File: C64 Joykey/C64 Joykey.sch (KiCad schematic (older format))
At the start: 30 parts, among them J1 Port_1, J2 Port_2, M1 Mounting, M2 Mounting, M3 Mounting, M4 Mounting, SW1 FIRE1, SW2 FIRE2, SW3 FIRE3, SW4 UP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

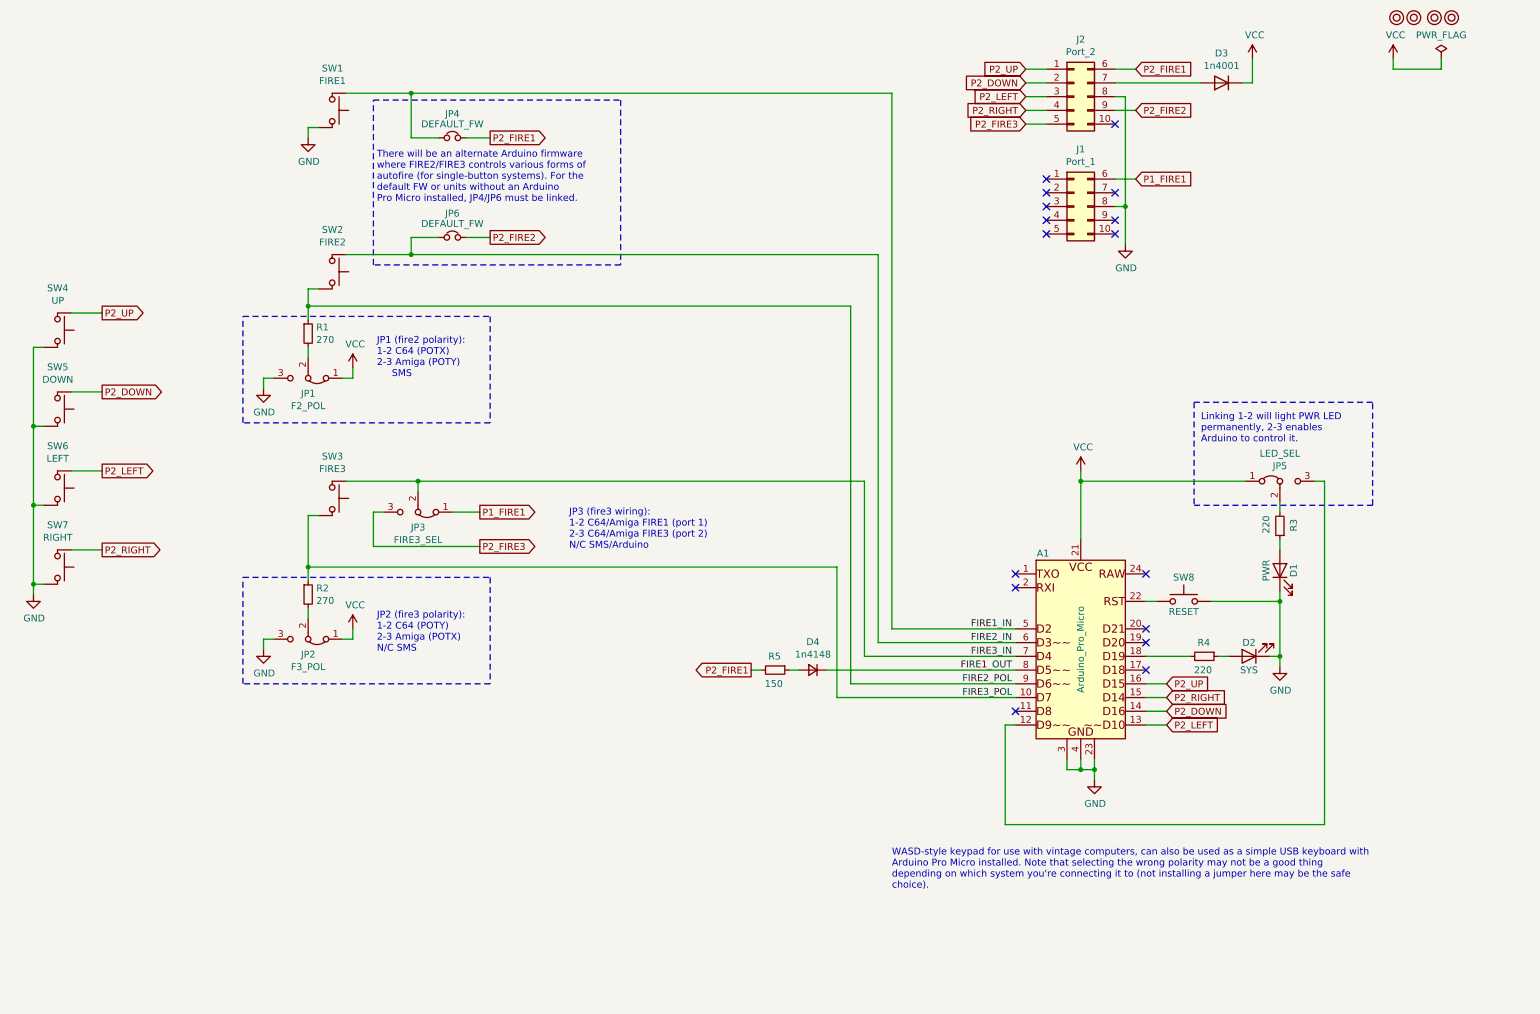
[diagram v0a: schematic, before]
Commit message: Underglow LEDs added
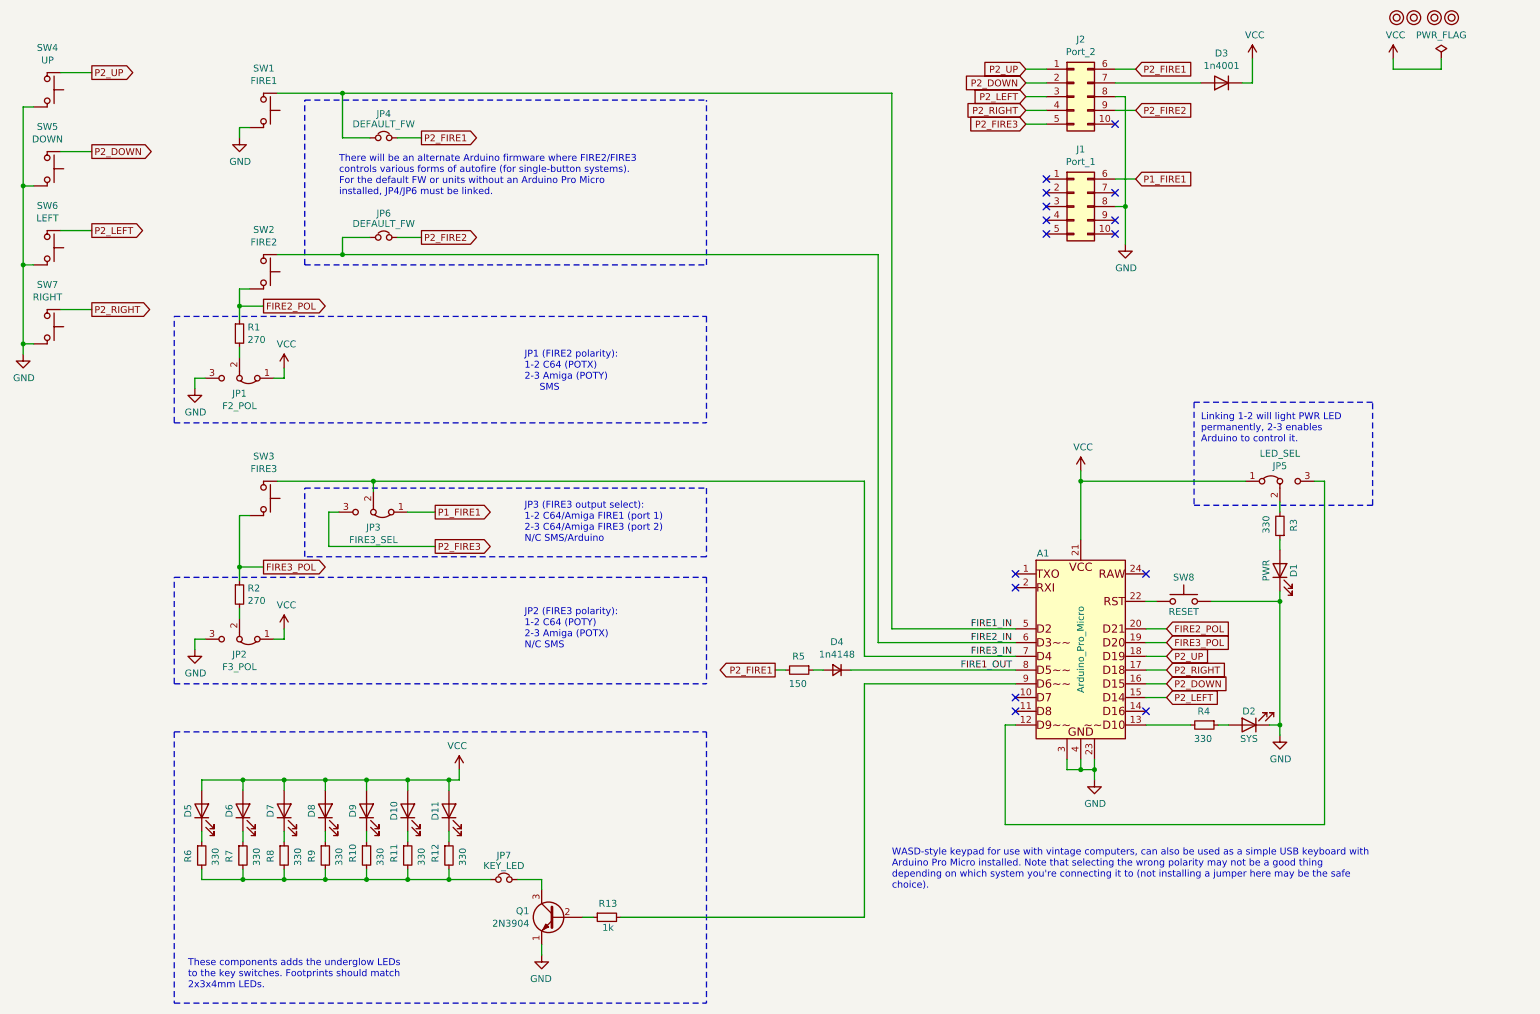
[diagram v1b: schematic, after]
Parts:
- added D10, D11, D5, D6, D7, D8, D9: LED, LED_THT:LED_Rectangular_W3.0mm_H2.0mm, symbol Device:LED
- added JP7: KEY_LED, Connector_PinHeader_2.54mm:PinHeader_1x02_P2.54mm_Horizontal, symbol Device:Jumper_NC_Small
- added Q1: 2N3904, Package_TO_SOT_THT:TO-92_Inline_W4.0mm_Horizontal_FlatSideDown, symbol Transistor_BJT:2N3904
- added R10, R11, R12, R6, R7, R8, R9: 330, Resistor_THT:R_Axial_DIN0207_L6.3mm_D2.5mm_P10.16mm_Horizontal, symbol Device:R_Small
- added R13: 1k, Resistor_THT:R_Axial_DIN0207_L6.3mm_D2.5mm_P10.16mm_Horizontal, symbol Device:R_Small
- JP4, JP6: footprint Pin_Headers:Pin_Header_Straight_1x02_Pitch2.54mm -> Connector_PinHeader_2.54mm:PinHeader_1x02_P2.54mm_Vertical
- R1, R2: footprint Resistors_THT:R_Axial_DIN0207_L6.3mm_D2.5mm_P10.16mm_Horizontal -> Resistor_THT:R_Axial_DIN0207_L6.3mm_D2.5mm_P10.16mm_Horizontal
- R3, R4: value 220 -> 330; footprint Resistors_THT:R_Axial_DIN0207_L6.3mm_D2.5mm_P10.16mm_Horizontal -> Resistor_THT:R_Axial_DIN0207_L6.3mm_D2.5mm_P10.16mm_Horizontal
- R5: footprint Resistors_THT:R_Axial_DIN0207_L6.3mm_D2.5mm_P7.62mm_Horizontal -> Resistor_THT:R_Axial_DIN0207_L6.3mm_D2.5mm_P7.62mm_Horizontal
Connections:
- net FIRE2_POL: now also A1.20 (D21); no longer A1.9 (D6)
- net FIRE3_POL: now also A1.19 (D20); no longer A1.10 (D7)
- net GND: now also Q1.1 (E)
- net P2_DOWN: now also A1.16 (D15); no longer A1.14 (D16)
- net P2_LEFT: now also A1.15 (D14); no longer A1.13 (D10)
- net P2_RIGHT: now also A1.17 (D18); no longer A1.15 (D14)
- net P2_UP: now also A1.18 (D19); no longer A1.16 (D15)
- net VCC: now also D10.2 (A), D11.2 (A), D5.2 (A), D6.2 (A), D7.2 (A), D8.2 (A), D9.2 (A)
- net at R4.2: now also A1.13 (D10); no longer A1.18 (D19)
- new net: A1.9 (D6), R13.2
- new net: D11.1 (K), R12.1
- new net: Q1.2 (B), R13.1
- new net: JP7.2, Q1.3 (C)
- new net: D10.1 (K), R11.1
- new net: D9.1 (K), R10.1
- new net: D8.1 (K), R9.1
- new net: D7.1 (K), R8.1
- new net: D6.1 (K), R7.1
- new net: D5.1 (K), R6.1
- new net: JP7.1, R10.2, R11.2, R12.2, R6.2, R7.2, R8.2, R9.2
- no-connect marks 16 -> 15
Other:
- note added: "JP1 (FIRE2 polarity):\n1-2 C64 (POTX)\n2-3 Amiga (POTY)\n SMS\n"
- note added: "JP2 (FIRE3 polarity):\n1-2 C64 (POTY)\n2-3 Amiga (POTX)\nN/C SMS\n"
- note added: "JP3 (FIRE3 output select):\n1-2 C64/Amiga FIRE1 (port 1)\n2-3 C64/Amiga FIRE3 (port 2)\nN/C SMS/Arduino"
- note added: "There will be an alternate Arduino firmware where FIRE2/FIRE3\ncontrols various forms of autofire (for single-button systems).\nFor the default FW or units without an Arduino Pro Micro \ninstalled, JP4/JP6 must be linked."
- note added: "These components adds the underglow LEDs\nto the key switches. Footprints should match\n2x3x4mm LEDs."
- note removed: "JP1 (fire2 polarity):\n1-2 C64 (POTX)\n2-3 Amiga (POTY)\n SMS\n"
- note removed: "JP2 (fire3 polarity):\n1-2 C64 (POTY)\n2-3 Amiga (POTX)\nN/C SMS\n"
- note removed: "JP3 (fire3 wiring):\n1-2 C64/Amiga FIRE1 (port 1)\n2-3 C64/Amiga FIRE3 (port 2)\nN/C SMS/Arduino"
- note removed: "There will be an alternate Arduino firmware\nwhere FIRE2/FIRE3 controls various forms of\nautofire (for single-button systems). For the\ndefault FW or units without an Arduino\nPro Micro installed, JP4/JP6 must be linked."
- moved on the sheet: D2, D4, JP1, JP2, JP3, JP4, JP6, R1, R2, R4, R5, SW1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

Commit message: Changed Q1 footprint
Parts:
- Q1: footprint Package_TO_SOT_THT:TO-92_Inline_W4.0mm_Horizontal_FlatSideDown -> 2n3904:2N3904_TO-92_Horizontal_FlatSideDown
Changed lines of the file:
@@
 F 0 "Q1" H 4765 7146 50  0000 L CNN
 F 1 "2N3904" H 4765 7055 50  0000 L CNN
-F 2 "Package_TO_SOT_THT:TO-92_Inline_W4.0mm_Horizontal_FlatSideDown" H 4775 7025 50  0001 L CIN
+F 2 "2n3904:2N3904_TO-92_Horizontal_FlatSideDown" H 4775 7025 50  0001 L CIN
 F 3 "https://www.onsemi.com/pub/Collateral/2N3903-D.PDF" H 4575 7100 50  0001 L CNN
 	1    4575 7100

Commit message: Flipped MX-switches
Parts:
- added D12: 1n4148, Diode_THT:D_DO-35_SOD27_P7.62mm_Horizontal, symbol Device:D_Small
- added R14: 150, Resistor_THT:R_Axial_DIN0207_L6.3mm_D2.5mm_P10.16mm_Horizontal, symbol Device:R_Small
- D4: footprint Diodes_THT:D_DO-35_SOD27_P7.62mm_Horizontal -> Diode_THT:D_DO-35_SOD27_P7.62mm_Horizontal
- J1: symbol Connector_Generic:Conn_02x05_Top_Bottom -> c64_idc:C64_IDC2_OUT
- J2: symbol c64_idc:c64_idc -> c64_idc:C64_IDC2_OUT
- R5: footprint Resistor_THT:R_Axial_DIN0207_L6.3mm_D2.5mm_P7.62mm_Horizontal -> Resistor_THT:R_Axial_DIN0207_L6.3mm_D2.5mm_P10.16mm_Horizontal
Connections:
- net P2_FIRE2: now also R14.2
- net FIRE2_OUT: now reaches A1.10 (D7)
- net FIRE2_OUT: now also D12.1 (K)
- net PWR: now reaches A1.12 (D9), JP5.3 (B)
- net SYS: now reaches A1.13 (D10), R4.2
- net UNDERGLOW: now reaches A1.9 (D6), R13.2
- new net: D12.2 (A), R14.1
- no-connect marks 15 -> 12
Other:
- note added: "These components adds the underglow LEDs to the key\nswitches. Footprints should match 2x3x4mm LEDs.\nStandard 3mm should also work with Gateron switches."
- note removed: "These components adds the underglow LEDs\nto the key switches. Footprints should match\n2x3x4mm LEDs."
- moved on the sheet: D3
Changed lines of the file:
@@
 	2275 1350 2350 1350
 $Comp
-L Connector_Generic:Conn_02x05_Top_Bottom J1
+L c64_idc:C64_IDC2_OUT J1
 U 1 1 5FB76154
-P 8350 1925
-F 0 "J1" H 8400 2342 50  0000 C CNN
-F 1 "Port_1" H 8400 2251 50  0000 C CNN
-F 2 "C64 IDC:IDC_Joystick" H 8350 1925 50  0001 C CNN
-F 3 "~" H 8350 1925 50  0001 C CNN
-	1    8350 1925
+P 8350 2200
+F 0 "J1" H 8400 2617 50  0000 C CNN
+F 1 "Port_1" H 8400 2526 50  0000 C CNN
+F 2 "C64 IDC:IDC_Joystick" H 8350 2200 50  0001 C CNN
+F 3 "~" H 8350 2200 50  0001 C CNN
+	1    8350 2200
 	1    0    0    -1
 $EndComp
@@
 L power:GND #PWR03
 U 1 1 5FB76300
-P 8725 2200
-F 0 "#PWR03" H 8725 1950 50  0001 C CNN
-F 1 "GND" H 8730 2027 50  0000 C CNN
-F 2 "" H 8725 2200 50  0001 C CNN
-F 3 "" H 8725 2200 50  0001 C CNN
-	1    8725 2200
-	1    0    0    -1
-$EndComp
-NoConn ~ 8650 1325
-NoConn ~ 8650 2125
-Wire Wire Line
-	8650 1725 8800 1725
-Text GLabel 8800 925  2    50   Input ~ 0
+P 8900 2475
+F 0 "#PWR03" H 8900 2225 50  0001 C CNN
+F 1 "GND" H 8905 2302 50  0000 C CNN
+F 2 "" H 8900 2475 50  0001 C CNN
+F 3 "" H 8900 2475 50  0001 C CNN
+	1    8900 2475
+	1    0    0    -1
+$EndComp
+Wire Wire Line
+	8825 2000 8975 2000
+Text GLabel 8975 1200 2    50   Input ~ 0
 P2_FIRE1
-Text GLabel 8800 1725 2    50   Input ~ 0
+Text GLabel 8975 2000 2    50   Input ~ 0
 P1_FIRE1
 $Comp
 L power:VCC #PWR02
 U 1 1 5FB781A5
-P 9650 850
-F 0 "#PWR02" H 9650 700 50  0001 C CNN
-F 1 "VCC" H 9667 1023 50  0000 C CNN
-F 2 "" H 9650 850 50  0001 C CNN
-F 3 "" H 9650 850 50  0001 C CNN
-	1    9650 850
-	1    0    0    -1
-$EndComp
-NoConn ~ 8150 1725
-NoConn ~ 8150 1825
-NoConn ~ 8150 1925
-NoConn ~ 8150 2025
-NoConn ~ 8150 2125
-NoConn ~ 8650 1825
-Text GLabel 8000 925  0    50   Input ~ 0
+P 9825 1125
+F 0 "#PWR02" H 9825 975 50  0001 C CNN
+F 1 "VCC" H 9842 1298 50  0000 C CNN
+F 2 "" H 9825 1125 50  0001 C CNN
+F 3 "" H 9825 1125 50  0001 C CNN
+	1    9825 1125
+	1    0    0    -1
+$EndComp
+NoConn ~ 7900 2000
+NoConn ~ 7900 2100
+NoConn ~ 7900 2200
+NoConn ~ 7900 2300
+NoConn ~ 7900 2400
+NoConn ~ 8825 2100
+Text GLabel 7750 1200 0    50   Input ~ 0
 P2_UP
 Wire Wire Line
-	8000 925  8150 925
-Text GLabel 8000 1025 0    50   Input ~ 0
+	7750 1200 7900 1200
+Text GLabel 7750 1300 0    50   Input ~ 0
 P2_DOWN
 Wire Wire Line
-	8150 1025 8000 1025
-Text GLabel 8000 1125 0    50   Input ~ 0
+	7900 1300 7750 1300
+Text GLabel 7750 1400 0    50   Input ~ 0
 P2_LEFT
 Wire Wire Line
-	8000 1125 8150 1125
-Text GLabel 8000 1225 0    50   Input ~ 0
+	7750 1400 7900 1400
+Text GLabel 7750 1500 0    50   Input ~ 0
 P2_RIGHT
 Wire Wire Line
-	8000 1225 8150 1225
-Text GLabel 8800 1225 2    50   Input ~ 0
+	7750 1500 7900 1500
+Text GLabel 8975 1500 2    50   Input ~ 0
 P2_FIRE2
 Wire Wire Line
-	8800 1225 8650 1225
-Text GLabel 8000 1325 0    50   Input ~ 0
+	8975 1500 8825 1500
+Text GLabel 7750 1600 0    50   Input ~ 0
 P2_FIRE3
 Wire Wire Line
-	8000 1325 8150 1325
+	7750 1600 7900 1600
 $Comp
 L sw_keyboard:SW_Keyboard SW4
@@
 P2_FIRE1
 Wire Wire Line
-	8650 1925 8725 1925
-Connection ~ 8725 1925
-Wire Wire Line
-	8725 1925 8725 2200
-NoConn ~ 8650 2025
-Wire Wire Line
-	8650 1125 8725 1125
-Wire Wire Line
-	8725 1125 8725 1925
-Wire Wire Line
-	9650 1025 9650 850
+	8825 2200 8900 2200
+Connection ~ 8900 2200
+Wire Wire Line
+	8900 2200 8900 2475
+NoConn ~ 8825 2300
+Wire Wire Line
+	8825 1400 8900 1400
+Wire Wire Line
+	8900 1400 8900 2200
+Wire Wire Line
+	9825 1300 9825 1125
 Text GLabel 9025 5300 2    50   Input ~ 0
 P2_RIGHT
@@
 	8400 3925 9600 3925
 Wire Wire Line
-	7925 5700 7850 5700
-Wire Wire Line
-	7850 5700 7850 6425
-Wire Wire Line
-	7850 6425 10175 6425
-Wire Wire Line
 	10175 6425 10175 3925
 Wire Wire Line
@@
 L Device:D D3
 U 1 1 5FCFF93E
-P 9425 1025
-F 0 "D3" H 9425 809 50  0000 C CNN
-F 1 "1n4001" H 9425 900 50  0000 C CNN
-F 2 "Diodes_THT:D_DO-41_SOD81_P10.16mm_Horizontal" H 9425 1025 50  0001 C CNN
-F 3 "~" H 9425 1025 50  0001 C CNN
-	1    9425 1025
+P 9600 1300
+F 0 "D3" H 9600 1084 50  0000 C CNN
+F 1 "1n4001" H 9600 1175 50  0000 C CNN
+F 2 "Diodes_THT:D_DO-41_SOD81_P10.16mm_Horizontal" H 9600 1300 50  0001 C CNN
+F 3 "~" H 9600 1300 50  0001 C CNN
+	1    9600 1300
 	-1   0    0    1
 $EndComp
 Wire Wire Line
-	8650 925  8800 925
-Wire Wire Line
-	9575 1025 9650 1025
-Wire Wire Line
-	8650 1025 9275 1025
+	8825 1200 8975 1200
+Wire Wire Line
+	9750 1300 9825 1300
+Wire Wire Line
+	8825 1300 9450 1300
 $Comp
 L power:PWR_FLAG #FLG0101
@@
 U 1 1 5FD49B7F
 P 6625 5300
-F 0 "D4" H 6625 5095 50  0000 C CNN
-F 1 "1n4148" H 6625 5186 50  0000 C CNN
-F 2 "Diodes_THT:D_DO-35_SOD27_P7.62mm_Horizontal" V 6625 5300 50  0001 C CNN
+F 0 "D4" H 6625 5125 50  0000 C CNN
+F 1 "1n4148" H 6625 5200 50  0000 C CNN
+F 2 "Diode_THT:D_DO-35_SOD27_P7.62mm_Horizontal" V 6625 5300 50  0001 C CNN
 F 3 "~" V 6625 5300 50  0001 C CNN
 	1    6625 5300
@@
 U 1 1 5FDC0E14
 P 6350 5300
-F 0 "R5" V 6250 5250 50  0000 L CNN
-F 1 "150" V 6450 5225 50  0000 L CNN
-F 2 "Resistor_THT:R_Axial_DIN0207_L6.3mm_D2.5mm_P7.62mm_Horizontal" H 6350 5300 50  0001 C CNN
+F 0 "R5" V 6175 5250 50  0000 L CNN
+F 1 "150" V 6250 5225 50  0000 L CNN
+F 2 "Resistor_THT:R_Axial_DIN0207_L6.3mm_D2.5mm_P10.16mm_Horizontal" H 6350 5300 50  0001 C CNN
 F 3 "~" H 6350 5300 50  0001 C CNN
 	1    6350 5300
@@
 	6175 5300 6250 5300
 $Comp
-L c64_idc:c64_idc J2
+L c64_idc:C64_IDC2_OUT J2
 U 1 1 5FB748C4
-P 8350 1125
-F 0 "J2" H 8400 1542 50  0000 C CNN
-F 1 "Port_2" H 8400 1451 50  0000 C CNN
-F 2 "C64 IDC:IDC_Joystick" H 8350 1125 50  0001 C CNN
-F 3 "~" H 8350 1125 50  0001 C CNN
-	1    8350 1125
+P 8350 1400
+F 0 "J2" H 8400 1817 50  0000 C CNN
+F 1 "Port_2" H 8400 1726 50  0000 C CNN
+F 2 "C64 IDC:IDC_Joystick" H 8350 1400 50  0001 C CNN
+F 3 "~" H 8350 1400 50  0001 C CNN
+	1    8350 1400
 	1    0    0    -1
 $EndComp
@@
 Wire Wire Line
 	8875 5100 9025 5100
-NoConn ~ 7925 5500
 Wire Wire Line
 	6825 7100 6825 5400
@@
 	1800 5750 1800 7725
 Text Notes 1900 7625 0    50   ~ 0
-These components adds the underglow LEDs\nto the key switches. Footprints should match\n2x3x4mm LEDs.
+These components adds the underglow LEDs to the key\nswitches. Footprints should match 2x3x4mm LEDs.\nStandard 3mm should also work with Gateron switches.
 Wire Wire Line
 	3025 2275 6925 2275
@@
 Wire Wire Line
 	4300 6825 4475 6825
+Text GLabel 6175 5500 0    50   Output ~ 0
+P2_FIRE2
+$Comp
+L Device:D_Small D12
+U 1 1 600C6BE2
+P 6625 5500
+F 0 "D12" H 6625 5600 50  0000 C CNN
+F 1 "1n4148" H 6625 5675 50  0000 C CNN
+F 2 "Diode_THT:D_DO-35_SOD27_P7.62mm_Horizontal" V 6625 5500 50  0001 C CNN
+F 3 "~" V 6625 5500 50  0001 C CNN
+	1    6625 5500
+	-1   0    0    1
+$EndComp
+$Comp
+L Device:R_Small R14
+U 1 1 600C6BE8
+P 6350 5500
+F 0 "R14" V 6450 5450 50  0000 L CNN
+F 1 "150" V 6525 5425 50  0000 L CNN
+F 2 "Resistor_THT:R_Axial_DIN0207_L6.3mm_D2.5mm_P10.16mm_Horizontal" H 6350 5500 50  0001 C CNN
+F 3 "~" H 6350 5500 50  0001 C CNN
+	1    6350 5500
+	0    1    1    0
+$EndComp
+Wire Wire Line
+	6450 5500 6525 5500
+Wire Wire Line
+	6175 5500 6250 5500
+Wire Wire Line
+	6725 5500 7925 5500
+Text Label 7900 5500 2    50   ~ 0
+FIRE2_OUT
+Text Label 8900 5700 0    50   ~ 0
+SYS
+Text Label 7900 5700 2    50   ~ 0
+PWR
+Wire Wire Line
+	7700 5700 7700 6425
+Wire Wire Line
+	7700 5700 7925 5700
+Wire Wire Line
+	7700 6425 10175 6425
+Text Label 7900 5400 2    50   ~ 0
+UNDERGLOW
 $EndSCHEMATC

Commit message: Added VCC_EN jumper
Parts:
- added JP8: VCC_EN, Connector_PinHeader_2.54mm:PinHeader_1x02_P2.54mm_Vertical, symbol Device:Jumper_NC_Small
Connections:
- net at J2.7 (Pin_7): now also JP8.1; no longer D3.2 (A)
- new net: D3.2 (A), JP8.2
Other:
- moved on the sheet: D3
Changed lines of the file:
@@
 L power:VCC #PWR02
 U 1 1 5FB781A5
-P 9825 1125
-F 0 "#PWR02" H 9825 975 50  0001 C CNN
-F 1 "VCC" H 9842 1298 50  0000 C CNN
-F 2 "" H 9825 1125 50  0001 C CNN
-F 3 "" H 9825 1125 50  0001 C CNN
-	1    9825 1125
+P 10325 1125
+F 0 "#PWR02" H 10325 975 50  0001 C CNN
+F 1 "VCC" H 10342 1298 50  0000 C CNN
+F 2 "" H 10325 1125 50  0001 C CNN
+F 3 "" H 10325 1125 50  0001 C CNN
+	1    10325 1125
 	1    0    0    -1
 $EndComp
@@
 	8900 1400 8900 2200
 Wire Wire Line
-	9825 1300 9825 1125
+	10325 1300 10325 1125
 Text GLabel 9025 5300 2    50   Input ~ 0
 P2_RIGHT
@@
 L Device:D D3
 U 1 1 5FCFF93E
-P 9600 1300
-F 0 "D3" H 9600 1084 50  0000 C CNN
-F 1 "1n4001" H 9600 1175 50  0000 C CNN
-F 2 "Diodes_THT:D_DO-41_SOD81_P10.16mm_Horizontal" H 9600 1300 50  0001 C CNN
-F 3 "~" H 9600 1300 50  0001 C CNN
-	1    9600 1300
+P 10100 1300
+F 0 "D3" H 10100 1084 50  0000 C CNN
+F 1 "1n4001" H 10100 1175 50  0000 C CNN
+F 2 "Diodes_THT:D_DO-41_SOD81_P10.16mm_Horizontal" H 10100 1300 50  0001 C CNN
+F 3 "~" H 10100 1300 50  0001 C CNN
+	1    10100 1300
 	-1   0    0    1
 $EndComp
@@
 	8825 1200 8975 1200
 Wire Wire Line
-	9750 1300 9825 1300
-Wire Wire Line
-	8825 1300 9450 1300
+	10250 1300 10325 1300
 $Comp
 L power:PWR_FLAG #FLG0101
@@
 Text Label 7900 5400 2    50   ~ 0
 UNDERGLOW
+$Comp
+L Device:Jumper_NC_Small JP8
+U 1 1 601EE585
+P 9675 1300
+F 0 "JP8" H 9675 1475 50  0000 C CNN
+F 1 "VCC_EN" H 9675 1400 50  0000 C CNN
+F 2 "Connector_PinHeader_2.54mm:PinHeader_1x02_P2.54mm_Vertical" H 9675 1300 50  0001 C CNN
+F 3 "~" H 9675 1300 50  0001 C CNN
+	1    9675 1300
+	1    0    0    -1
+$EndComp
+Wire Wire Line
+	9950 1300 9775 1300
+Wire Wire Line
+	8825 1300 9575 1300
 $EndSCHEMATC

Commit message: Added ARD_EN jumper
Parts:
- added JP9: ARD_EN, Connector_PinHeader_2.54mm:PinHeader_1x02_P2.54mm_Vertical, symbol Device:Jumper_NC_Small
- J2: symbol c64_idc:C64_IDC2_OUT -> c64_idc:C64_IDC2
- JP8: symbol Device:Jumper_NC_Small -> promicro:VCC_EN
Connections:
- net VCC: now also JP9.2; no longer A1.21 (VCC)
- new net: A1.21 (VCC), JP9.1
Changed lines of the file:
@@
 Wire Wire Line
 	8400 3925 8400 3850
-Connection ~ 8400 3925
 $Comp
 L Device:LED D2
@@
 	9850 4725 9850 4800
 Wire Wire Line
-	8400 3925 8400 4350
-Wire Wire Line
 	8400 3925 9600 3925
 Wire Wire Line
@@
 	6175 5300 6250 5300
 $Comp
-L c64_idc:C64_IDC2_OUT J2
+L c64_idc:C64_IDC2 J2
 U 1 1 5FB748C4
 P 8350 1400
@@
 UNDERGLOW
 $Comp
-L Device:Jumper_NC_Small JP8
+L promicro:VCC_EN JP8
 U 1 1 601EE585
 P 9675 1300
@@
 Wire Wire Line
 	8825 1300 9575 1300
+$Comp
+L Device:Jumper_NC_Small JP9
+U 1 1 6021387A
+P 8400 4125
+F 0 "JP9" H 8400 4300 50  0000 C CNN
+F 1 "ARD_EN" H 8400 4225 50  0000 C CNN
+F 2 "Connector_PinHeader_2.54mm:PinHeader_1x02_P2.54mm_Vertical" H 8400 4125 50  0001 C CNN
+F 3 "~" H 8400 4125 50  0001 C CNN
+	1    8400 4125
+	0    -1   -1   0
+$EndComp
+Wire Wire Line
+	8400 3925 8400 4025
+Connection ~ 8400 3925
+Wire Wire Line
+	8400 4225 8400 4350
 $EndSCHEMATC
